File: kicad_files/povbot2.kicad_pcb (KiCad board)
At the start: 2 copper layers, 65 x 30 mm, 5 parts, among them J1 GPIO

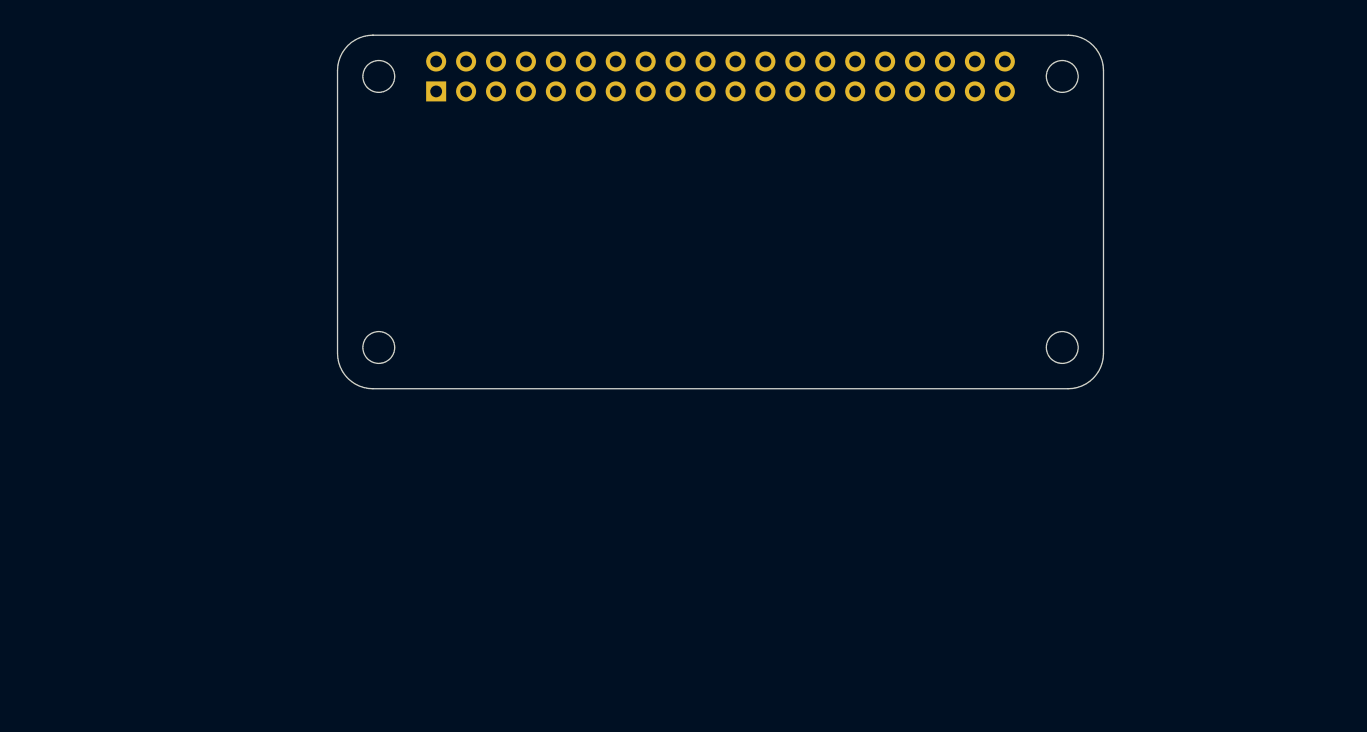
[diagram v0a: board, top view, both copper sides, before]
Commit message: started pcb, added foorprints etc
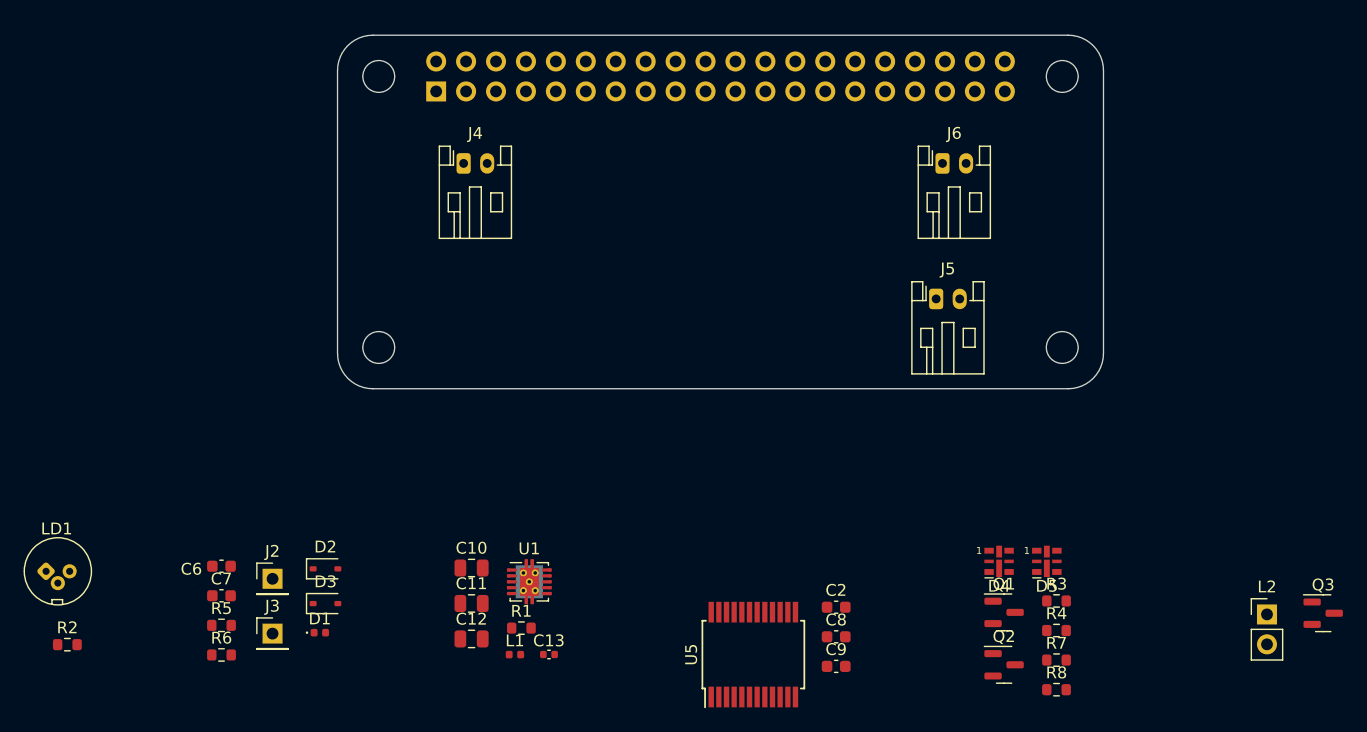
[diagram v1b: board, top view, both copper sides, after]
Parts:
- added C10: 22u, Capacitor_SMD:C_0805_2012Metric, F.Cu at (111.4, 115.2)
- added C11: 22u, Capacitor_SMD:C_0805_2012Metric, F.Cu at (111.4, 118.2)
- added C12: 22u, Capacitor_SMD:C_0805_2012Metric, F.Cu at (111.4, 121.2)
- added C13: 10n, Capacitor_SMD:C_0402_1005Metric, F.Cu at (117.9, 122.6)
- added C2: 0.1uF, Capacitor_SMD:C_0603_1608Metric, F.Cu at (142.3, 118.5)
- added C6: 4.7uF, Capacitor_SMD:C_0603_1608Metric, F.Cu at (90.2, 115.1)
- added C7: 4.7uF, Capacitor_SMD:C_0603_1608Metric, F.Cu at (90.2, 117.6)
- added C8: 10uF, Capacitor_SMD:C_0603_1608Metric, F.Cu at (142.3, 121.1)
- added C9: 10uF, Capacitor_SMD:C_0603_1608Metric, F.Cu at (142.3, 123.6)
- added D1: LED, LED_SMD:LED_0402_1005Metric, F.Cu at (98.5, 120.7)
- added D2: D_Schottky, Diode_SMD:D_SOD-323, F.Cu at (99.0, 115.3)
- added D3: D_Schottky, Diode_SMD:D_SOD-323, F.Cu at (99.0, 118.2)
- added D4: APA102-2020, LED_SMD:LED-APA102-2020, F.Cu at (156.1, 114.6)
- added D5: APA102-2020, LED_SMD:LED-APA102-2020, F.Cu at (160.2, 114.6)
- added J2: Conn_01x01, Connector_PinHeader_2.54mm:PinHeader_1x01_P2.54mm_Vertical, F.Cu at (94.5, 116.1)
- added J3: Conn_01x01, Connector_PinHeader_2.54mm:PinHeader_1x01_P2.54mm_Vertical, F.Cu at (94.5, 120.8)
- added J4: Conn_01x02, Connector_JST:JST_PH_S2B-PH-K_1x02_P2.00mm_Horizontal, F.Cu at (110.7, 80.9)
- added J5: Conn_01x02, Connector_JST:JST_PH_S2B-PH-K_1x02_P2.00mm_Horizontal, F.Cu at (150.8, 92.4)
- added J6: Conn_01x02, Connector_JST:JST_PH_S2B-PH-K_1x02_P2.00mm_Horizontal, F.Cu at (151.3, 80.9)
- added L1: 1uH, Inductor_SMD:L_0402_1005Metric, F.Cu at (115.1, 122.6)
- added L2: Electromagnet, Connector_PinHeader_2.54mm:PinHeader_1x02_P2.54mm_Vertical, F.Cu at (178.9, 119.2)
- added LD1: D_Laser_Photo_NType, OptoDevice:LaserDiode_TO18-D5.6-3, F.Cu at (75.3, 115.5)
- added Q1: BSS138, Package_TO_SOT_SMD:SOT-23, F.Cu at (156.6, 119.0)
- added Q2: BSS138, Package_TO_SOT_SMD:SOT-23, F.Cu at (156.6, 123.4)
- added Q3: BSS138, Package_TO_SOT_SMD:SOT-23, F.Cu at (183.6, 119.0)
- added R1: 1M, Resistor_SMD:R_0603_1608Metric, F.Cu at (115.6, 120.3)
- added R2: 68R, Resistor_SMD:R_0603_1608Metric, F.Cu at (77.1, 121.7)
- added R3: 10k, Resistor_SMD:R_0603_1608Metric, F.Cu at (161.0, 118.0)
- added R4: 10k, Resistor_SMD:R_0603_1608Metric, F.Cu at (161.0, 120.5)
- added R5: 470R, Resistor_SMD:R_0603_1608Metric, F.Cu at (90.2, 120.1)
- added R6: 2k, Resistor_SMD:R_0603_1608Metric, F.Cu at (90.2, 122.6)
- added R7: 10k, Resistor_SMD:R_0603_1608Metric, F.Cu at (161.0, 123.0)
- added R8: 10k, Resistor_SMD:R_0603_1608Metric, F.Cu at (161.0, 125.5)
- added U1: TPS61232DRC, Package_SON:Texas_S-PVSON-N10_ThermalVias, F.Cu at (116.3, 116.4)
- added U5: TB6612FNG, Package_SO:SSOP-24_5.3x8.2mm_P0.65mm, F.Cu at (135.3, 122.6)
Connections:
- J1 pad 32: /GPIO12/PWM0 -> unconnected-(J1-Pin_32-Pad32)
- J1 pad 33: /GPIO13/PWM1 -> unconnected-(J1-Pin_33-Pad33)

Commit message: floorplanning done
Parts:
- J4: footprint Connector_JST:JST_PH_S2B-PH-K_1x02_P2.00mm_Horizontal -> Connector_Molex:Molex_PicoBlade_53398-0271_1x02-1MP_P1.25mm_Vertical
- J5, J6: footprint Connector_JST:JST_PH_S2B-PH-K_1x02_P2.00mm_Horizontal -> Connector_Molex:Molex_PicoBlade_53261-0271_1x02-1MP_P1.25mm_Horizontal
- moved L2 79.1 mm to (104.6, 92.1), turned to -90 degrees
- moved D4 55.7 mm to (112.8, 79.6)
- moved Q1 52.9 mm to (120.4, 80.4)
- moved Q2 52.9 mm to (120.4, 84.9)
- moved R4 52.9 mm to (124.8, 82.0)
- moved R3 52.9 mm to (124.8, 79.5)
- moved R7 52.9 mm to (124.8, 84.5)
- moved R8 52.9 mm to (124.8, 87.0)
- moved D5 51.3 mm to (112.9, 94.7)
- moved R2 49.5 mm to (115.6, 90.7), turned to 90 degrees
- moved LD1 48.4 mm to (112.7, 84.8), turned to -90 degrees
- moved J5 47.7 mm to (103.6, 85.6), turned to -90 degrees
- moved C9 45.4 mm to (150.1, 78.8), turned to 90 degrees
- moved Q3 43.8 mm to (147.7, 94.1)
- moved C8 42.6 mm to (147.6, 78.8), turned to 90 degrees
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
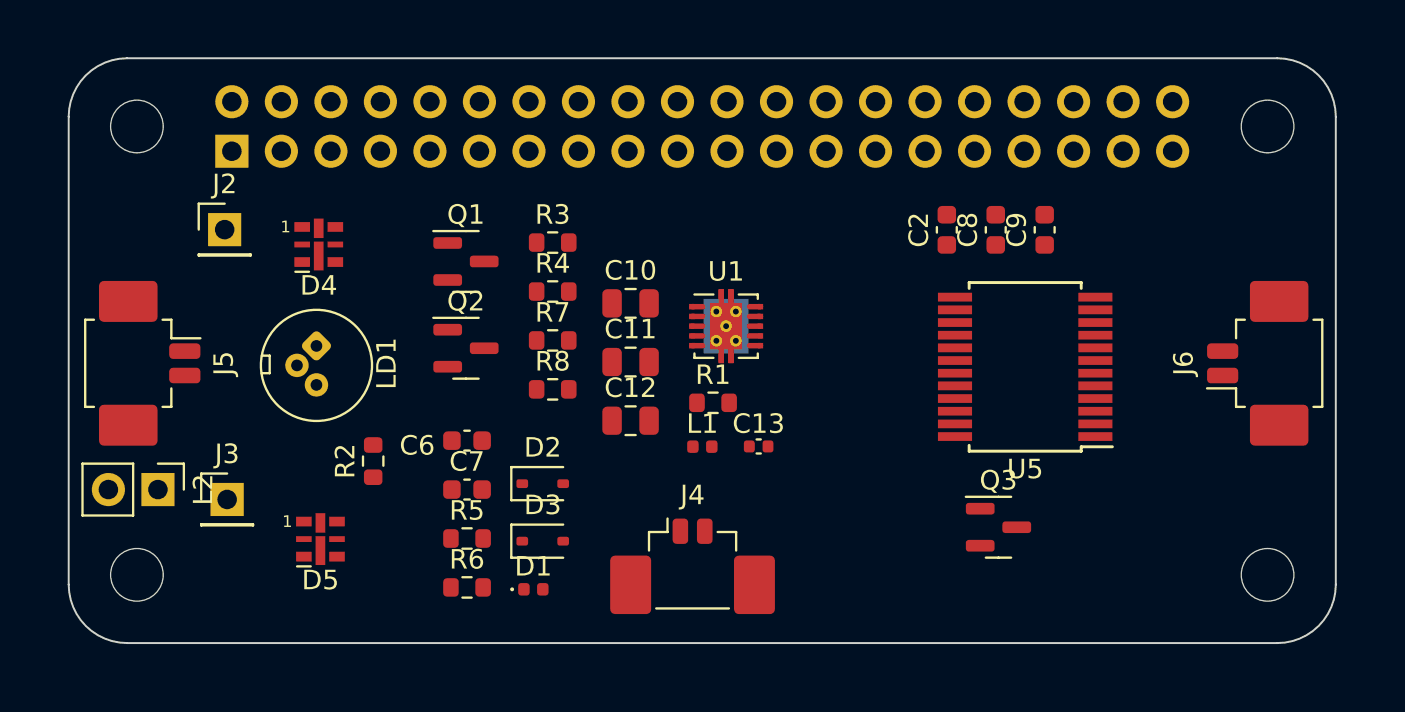
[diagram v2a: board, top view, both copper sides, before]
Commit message: changed inductor larger package 5A current version, made pcbway fab files
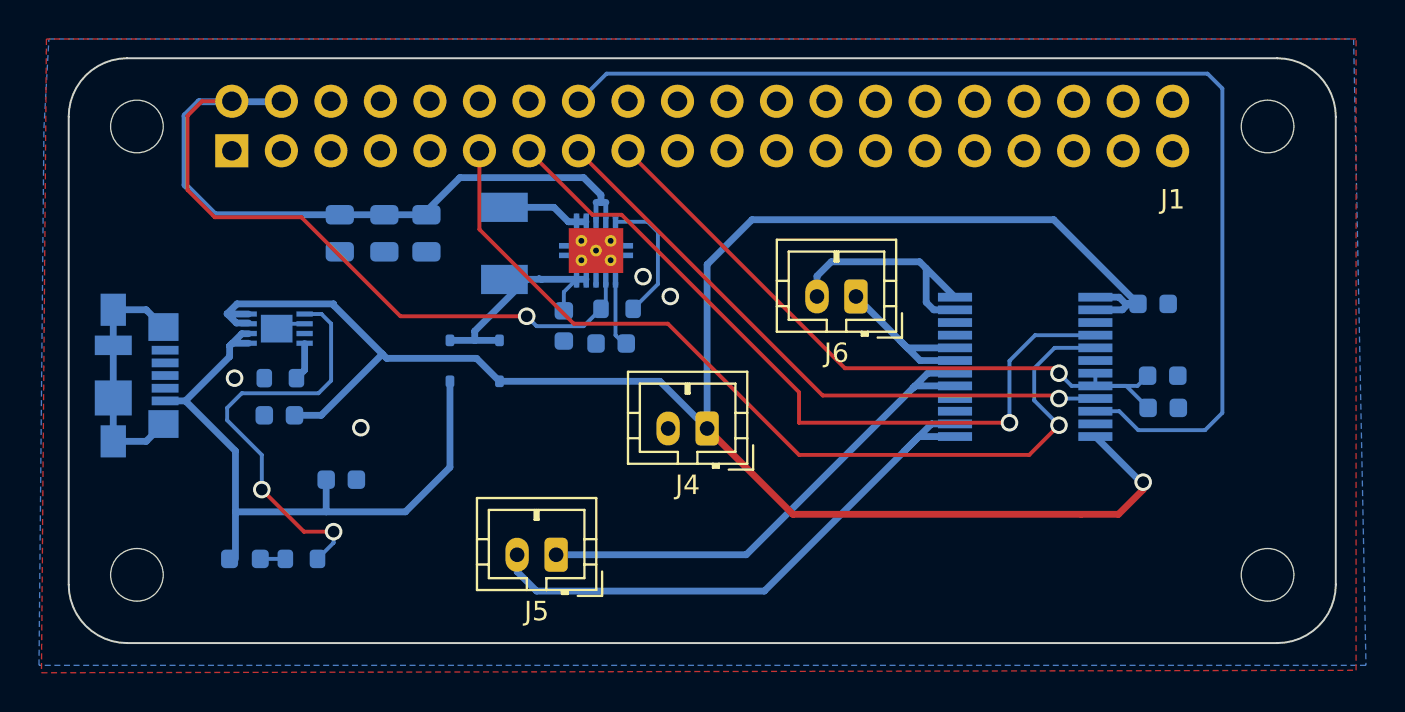
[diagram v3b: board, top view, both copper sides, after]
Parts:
- removed D4, D5: APA102-2020, LED_SMD:LED-APA102-2020
- removed J2, J3: Conn_01x01, Connector_PinHeader_2.54mm:PinHeader_1x01_P2.54mm_Vertical
- removed L2: Electromagnet, Connector_PinHeader_2.54mm:PinHeader_1x02_P2.54mm_Vertical
- removed LD1: D_Laser_Photo_NType, OptoDevice:LaserDiode_TO18-D5.6-3
- removed Q1, Q2, Q3: BSS138, Package_TO_SOT_SMD:SOT-23
- removed R2: 68R, Resistor_SMD:R_0603_1608Metric
- removed R3, R4, R7, R8: 10k, Resistor_SMD:R_0603_1608Metric
- added C1: 22u, Capacitor_SMD:C_0603_1608Metric, B.Cu at (125.4, 83.7)
- added J7: USB_B_Micro, Connector_USB:USB_Micro-B_Molex_47346-0001, B.Cu at (103.5, 86.3)
- added U4: MCP73831-2ACI_MC, Kicad_parts:SON50P200X300X100-9N, B.Cu at (110.7, 83.9)
- C10, C11, C12, C2, C6, C7, C8, C9, D2, D3, R1, R5, R6, U1, U5: moved to B.Cu
- C13: footprint Capacitor_SMD:C_0402_1005Metric -> Capacitor_SMD:C_0603_1608Metric; moved to B.Cu
- D1: footprint LED_SMD:LED_0402_1005Metric -> LED_SMD:LED_0603_1608Metric; moved to B.Cu
- J4: footprint Connector_Molex:Molex_PicoBlade_53398-0271_1x02-1MP_P1.25mm_Vertical -> Connector_JST:JST_PH_B2B-PH-K_1x02_P2.00mm_Vertical
- J5, J6: footprint Connector_Molex:Molex_PicoBlade_53261-0271_1x02-1MP_P1.25mm_Horizontal -> Connector_JST:JST_PH_B2B-PH-K_1x02_P2.00mm_Vertical
- L1: footprint Inductor_SMD:L_0402_1005Metric -> Kicad_parts:IND_SRP4020TA-1R0M; moved to B.Cu
- moved J5 23.6 mm to (125.0, 95.5), turned to 180 degrees
- moved J6 21.5 mm to (140.4, 82.2), turned to 180 degrees
- moved C11 16.3 mm to (113.9, 79.0), turned to 90 degrees
- moved D1 14.9 mm to (109.0, 95.7), turned to 180 degrees
- moved L1 14.6 mm to (122.4, 79.5), turned to 90 degrees
- moved R6 14.4 mm to (110.9, 86.4)
- moved C2 14.4 mm to (156.1, 87.9), turned to 0 degrees
- moved C12 14.2 mm to (118.4, 79.0), turned to 90 degrees
- moved C10 13.1 mm to (116.2, 79.0), turned to 90 degrees
- moved C8 11.4 mm to (156.1, 86.3), turned to 0 degrees
- moved C7 10.4 mm to (110.8, 88.3), turned to 180 degrees
- moved D3 9.51 mm to (122.1, 85.5), turned to -90 degrees
- moved C13 9.23 mm to (127.8, 84.6)
- moved R5 8.56 mm to (111.9, 95.7)
- moved D2 7.90 mm to (119.6, 85.5), turned to -90 degrees
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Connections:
- J1 pad 1: +3V3 -> unconnected-(J1-Pin_1-Pad1)
- U5 pad 19: unconnected-(U5-STBY-Pad19) -> +3V3
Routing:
- net +BATT: track 0.00 -> 102.2 mm, vias 0 -> 1
- net +5V: track 0.00 -> 67.1 mm, vias 0 -> 1
- net /GPIO23: track 0.00 -> 57.9 mm
- net /GPIO17: track 0.00 -> 46.2 mm, vias 0 -> 1
- net /GPIO27: track 0.00 -> 39.5 mm, vias 0 -> 1
- net +3V3: track 0.00 -> 35.7 mm, vias 0 -> 1
- net /VBUS: track 0.00 -> 34.3 mm
- net /GPIO22: track 0.00 -> 31.8 mm, vias 0 -> 1
- net /MOTORA_OUT2: track 0.00 -> 30.2 mm
- net /MOTORA_OUT1: track 0.00 -> 26.5 mm
- net Net-(U4-STAT): track 0.00 -> 21.6 mm, vias 0 -> 2
- net GND: track 0.00 -> 14.2 mm, vias 0 -> 4
- net /MOTORB_OUT1: track 0.00 -> 12.6 mm
- net Net-(D2-K): track 0.00 -> 11.9 mm
- net /MOTORB_OUT2: track 0.00 -> 9.38 mm
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- added copper zone on B.Cu, net GND
- added copper zone on F.Cu, net GND
